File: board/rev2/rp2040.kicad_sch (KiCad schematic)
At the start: 33 parts, among them J8 Conn_01x03, U13 TLV74311, U5 RP2354B, Y1 ABM8-272-T3

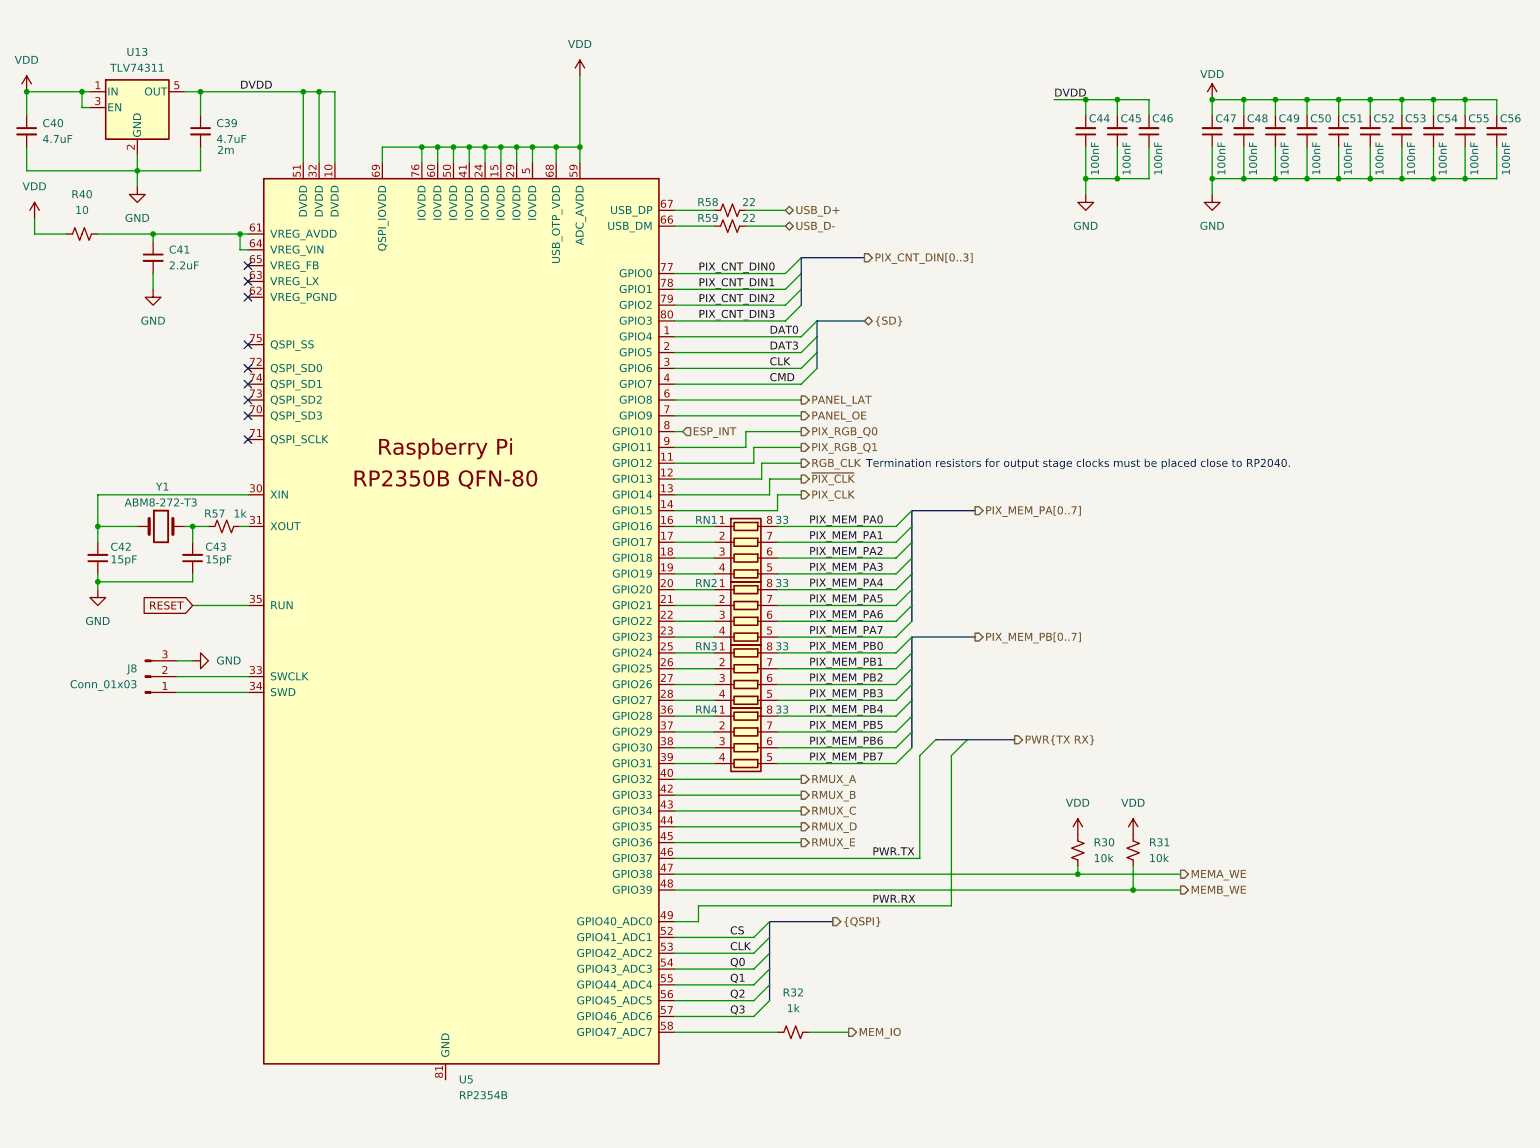
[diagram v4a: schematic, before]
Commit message: Start new PCB
- all footprints setup
- need to setup netclasses next, tho
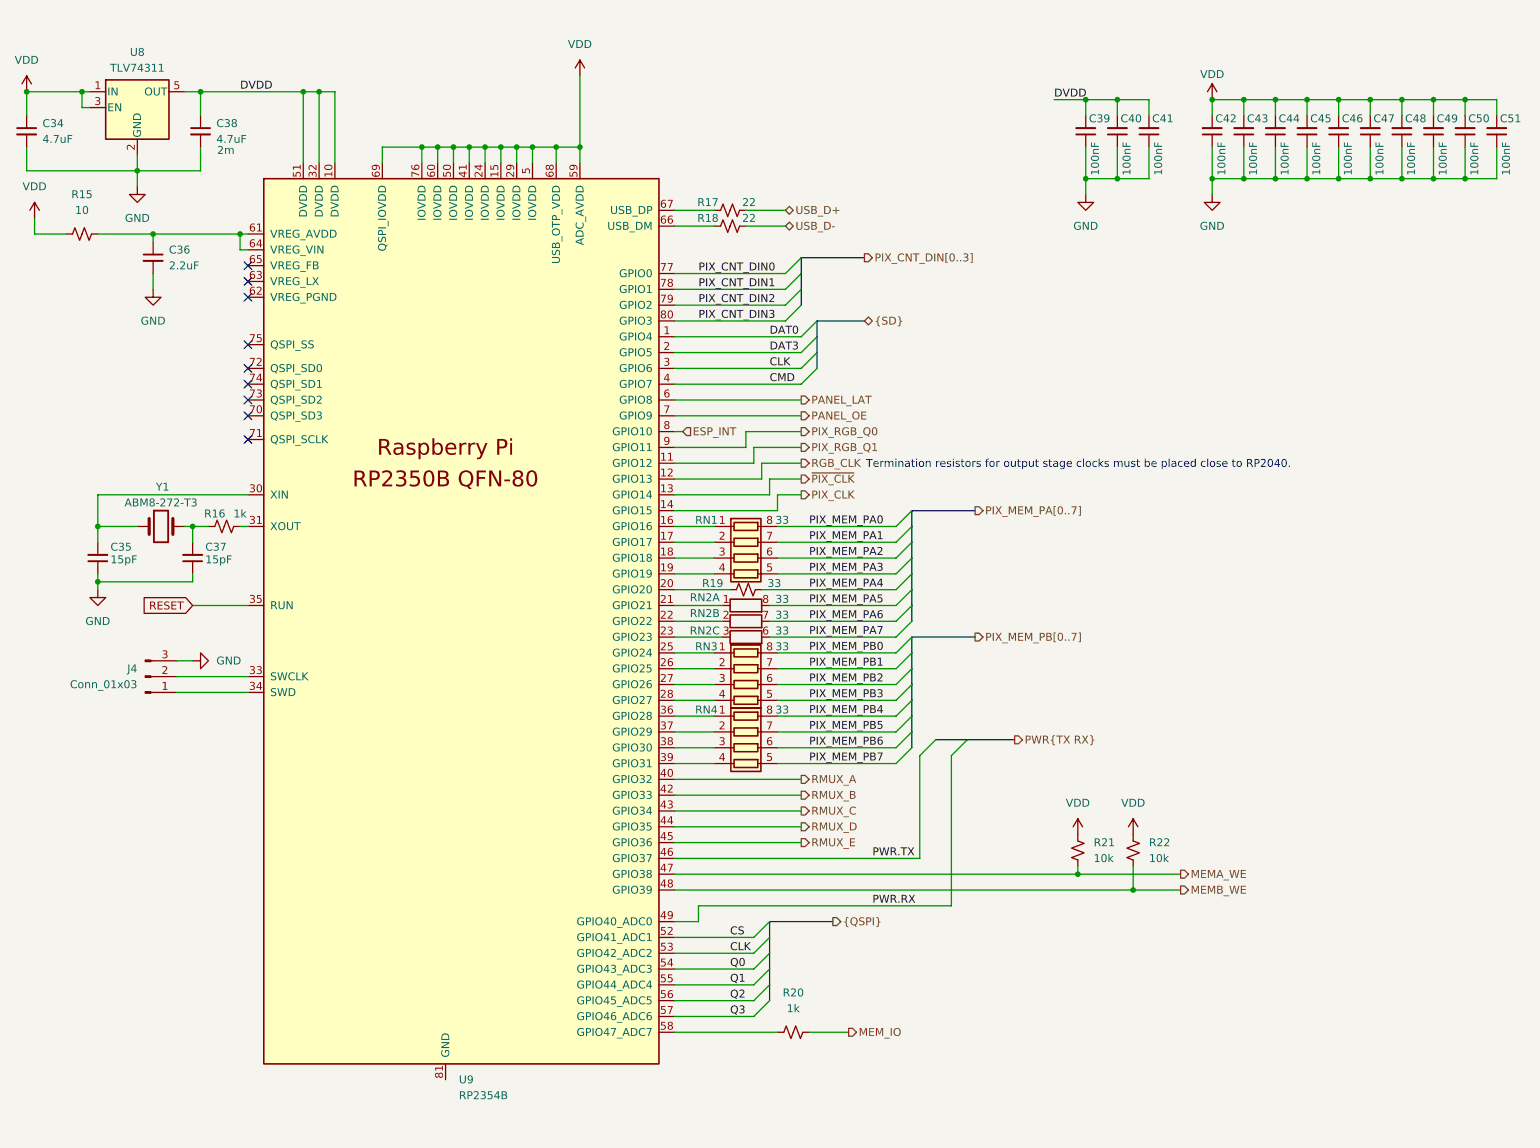
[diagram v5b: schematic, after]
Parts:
- removed RN2: 33, symbol Device:R_Pack04
- added R19: 33, Resistor_SMD:R_0402_1005Metric, symbol Device:R_Small_US
- added RN2: 33, RN_SMD:R_Array_Flat_4x0201, symbol Device:R_Pack04_Split
- RN1, RN3, RN4: footprint (none) -> RN_SMD:R_Array_Flat_4x0201; Part (none) -> YC104-FR-0733RL
- U8: renamed from U13; Part (none) -> TLV74311
- U9: renamed from U5; Part (none) -> RP2354B
- Y1: Part (none) -> ABM8-272-T3
- renumbered C40 to C34, C42 to C35, C41 to C36, C43 to C37, C39 to C38, C44 to C39, C45 to C40, C46 to C41, C47 to C42, C48 to C43, C49 to C44, C50 to C45, C51 to C46, C52 to C47, C53 to C48, C54 to C49, C55 to C50, C56 to C51, J8 to J4, R40 to R15, R57 to R16, R58 to R17, R59 to R18, R32 to R20, R30 to R21, R31 to R22
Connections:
- net PIX_MEM_PA4: now also R19.2
- net PIX_MEM_PA5: now also RN2.8 (R1.2)
- net PIX_MEM_PA6: now also RN2.7 (R2.2)
- net PIX_MEM_PA7: now also RN2.6 (R3.2)
- net at U9.20 (GPIO20): now also R19.1
- net at U9.21 (GPIO21): now also RN2.1 (R1.1)
- net at U9.22 (GPIO22): now also RN2.2 (R2.1)
- net at U9.23 (GPIO23): now also RN2.3 (R3.1)

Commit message: Add netclasses, more footprints, fix ERC
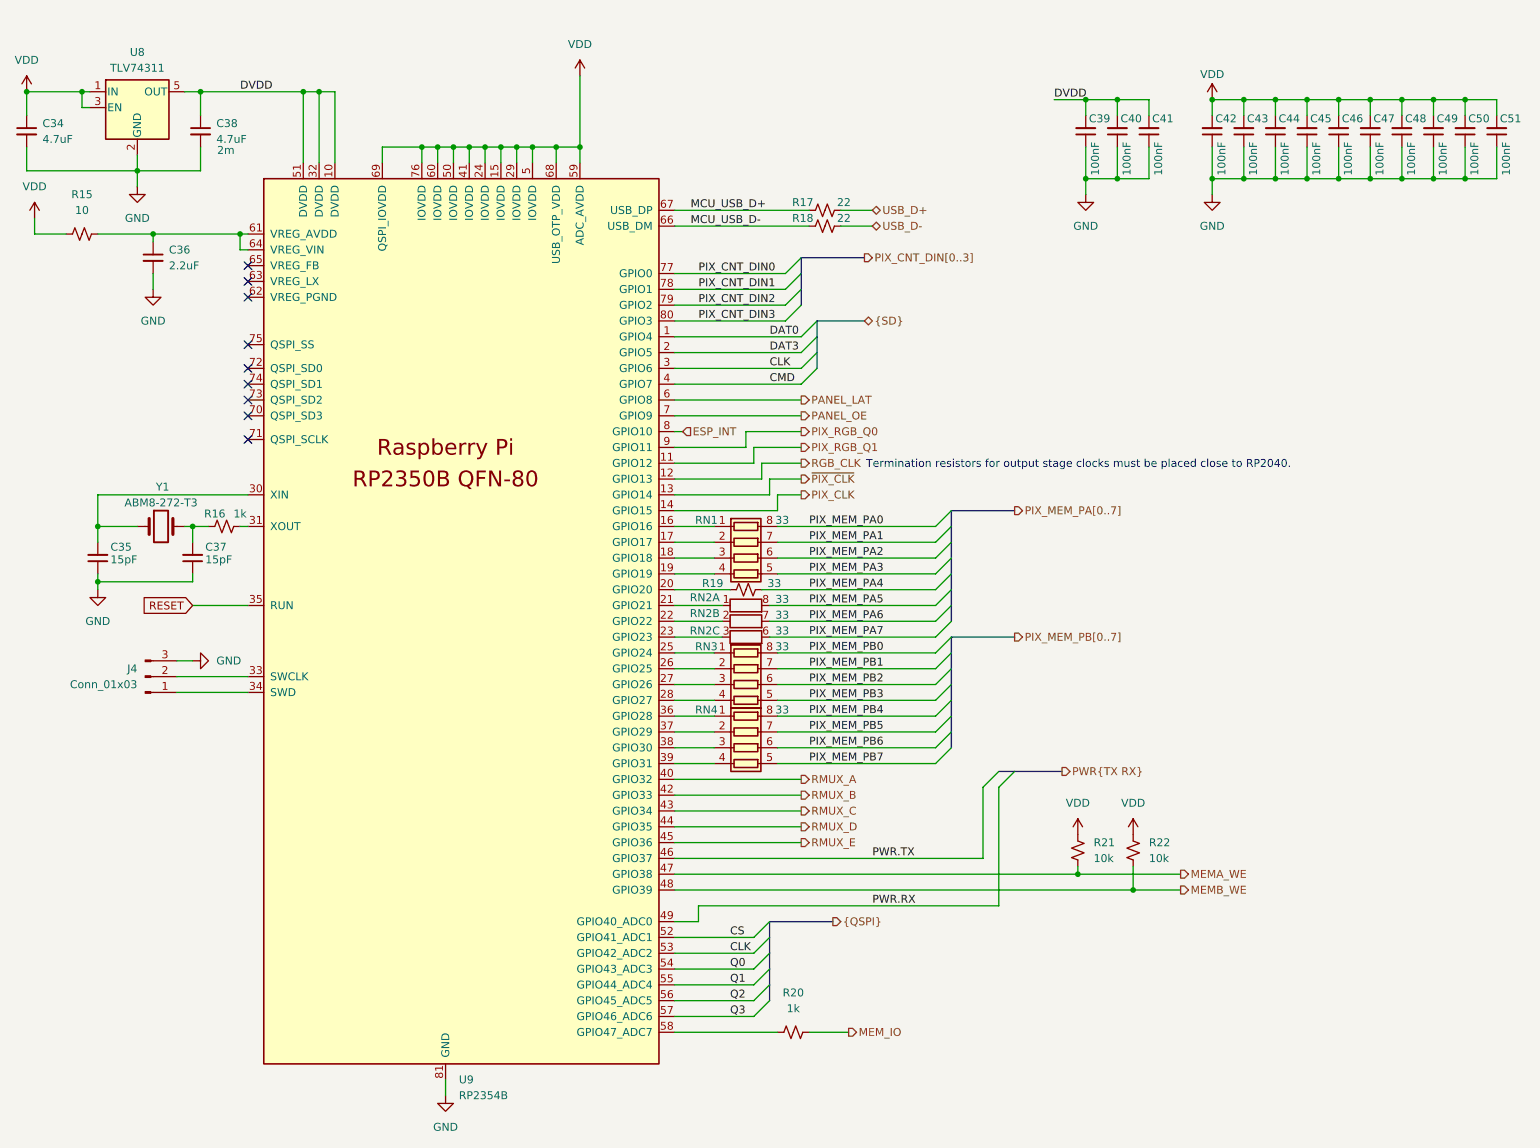
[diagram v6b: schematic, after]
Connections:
- net GND: now also U9.81 (GND)
- net MCU_USB_D+: now reaches R17.1, U9.67 (USB_DP)
- net MCU_USB_D-: now reaches R18.1, U9.66 (USB_DM)
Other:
- moved on the sheet: R17, R18

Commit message: Really finish rev2 board schematic
- fix some more footprints
  - move to real SD card holder, for example
- repair part numbers
- add LCSC part refs to everything
- add even more caps to the 3.3V reg output
  - really should use an LDO but meh it should be fine

total BOM cost for 5 of them is apparently 160 CAD, or like 32 dollars
each (don't think that includes the feeder fees tho)
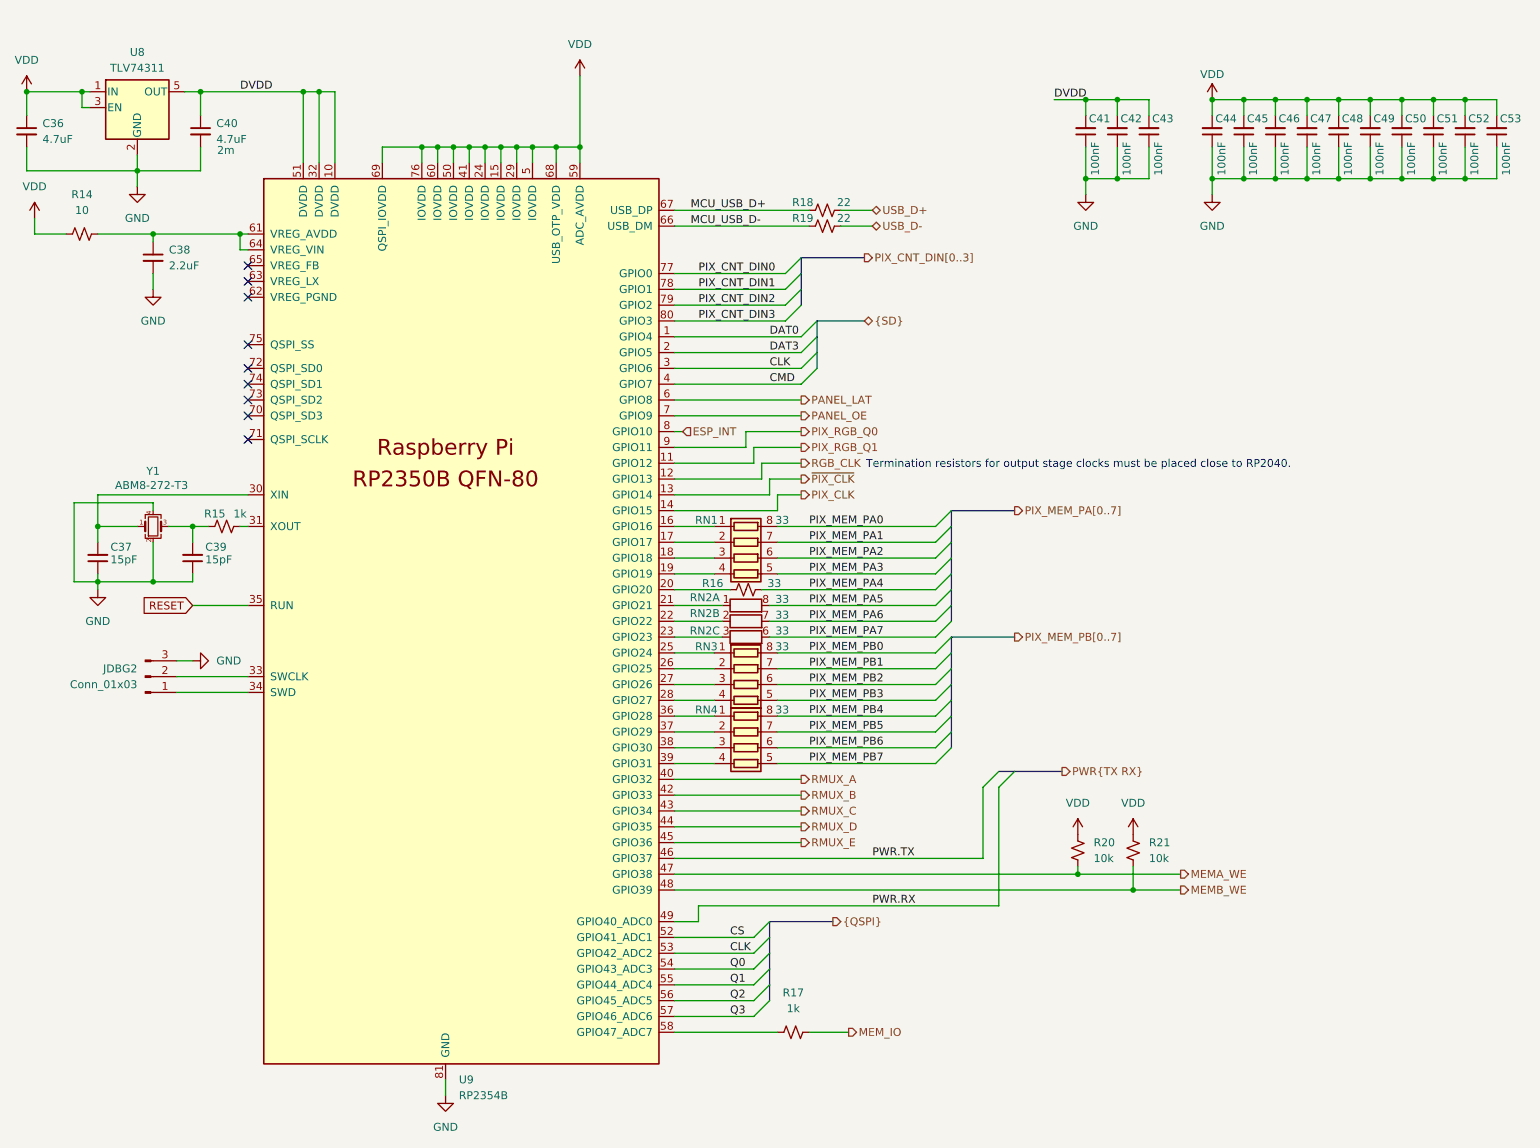
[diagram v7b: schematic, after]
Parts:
- C36: renamed from C34; LCSC (none) -> C29823
- C37: renamed from C35; LCSC (none) -> C1548
- C38: renamed from C36; LCSC (none) -> C23630
- C39: renamed from C37; LCSC (none) -> C1548
- C40: renamed from C38; LCSC (none) -> C29823
- C41: renamed from C39; LCSC (none) -> C307331
- C42: renamed from C40; LCSC (none) -> C307331
- C43: renamed from C41; LCSC (none) -> C307331
- C44: renamed from C42; LCSC (none) -> C307331
- C45: renamed from C43; LCSC (none) -> C307331
- C46: renamed from C44; LCSC (none) -> C307331
- C47: renamed from C45; LCSC (none) -> C307331
- C48: renamed from C46; LCSC (none) -> C307331
- C49: renamed from C47; LCSC (none) -> C307331
- C50: renamed from C48; LCSC (none) -> C307331
- C51: renamed from C49; LCSC (none) -> C307331
- C52: renamed from C50; LCSC (none) -> C307331
- C53: renamed from C51; LCSC (none) -> C307331
- R14: renamed from R15; LCSC (none) -> C25077
- R15: renamed from R16; LCSC (none) -> C11702
- R16: renamed from R19; LCSC (none) -> C25105
- R17: renamed from R20; LCSC (none) -> C11702
- R18: renamed from R17; LCSC (none) -> C25092
- R19: renamed from R18; LCSC (none) -> C25092
- R20: renamed from R21; LCSC (none) -> C17414
- R21: renamed from R22; LCSC (none) -> C17414
- RN1, RN2, RN3, RN4: LCSC (none) -> C854640
- U8: LCSC (none) -> C485147; Part TLV74311 -> TLV74311PDBVR
- U9: LCSC (none) -> C39843328
- Y1: symbol Device:Crystal -> Device:Crystal_GND24_Small; LCSC (none) -> C20625731
- renumbered J4 to JDBG2
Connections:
- net GND: now also Y1.2, Y1.4
- net at C39.2, R15.1: now also Y1.3; no longer Y1.2

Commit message: Start board
add a few extra bypass caps too, and swap some pins on the USB mux

i forgot to add a bypass cap on the tpd6s so that also needs to happen

truly 63 capacitors is not enough
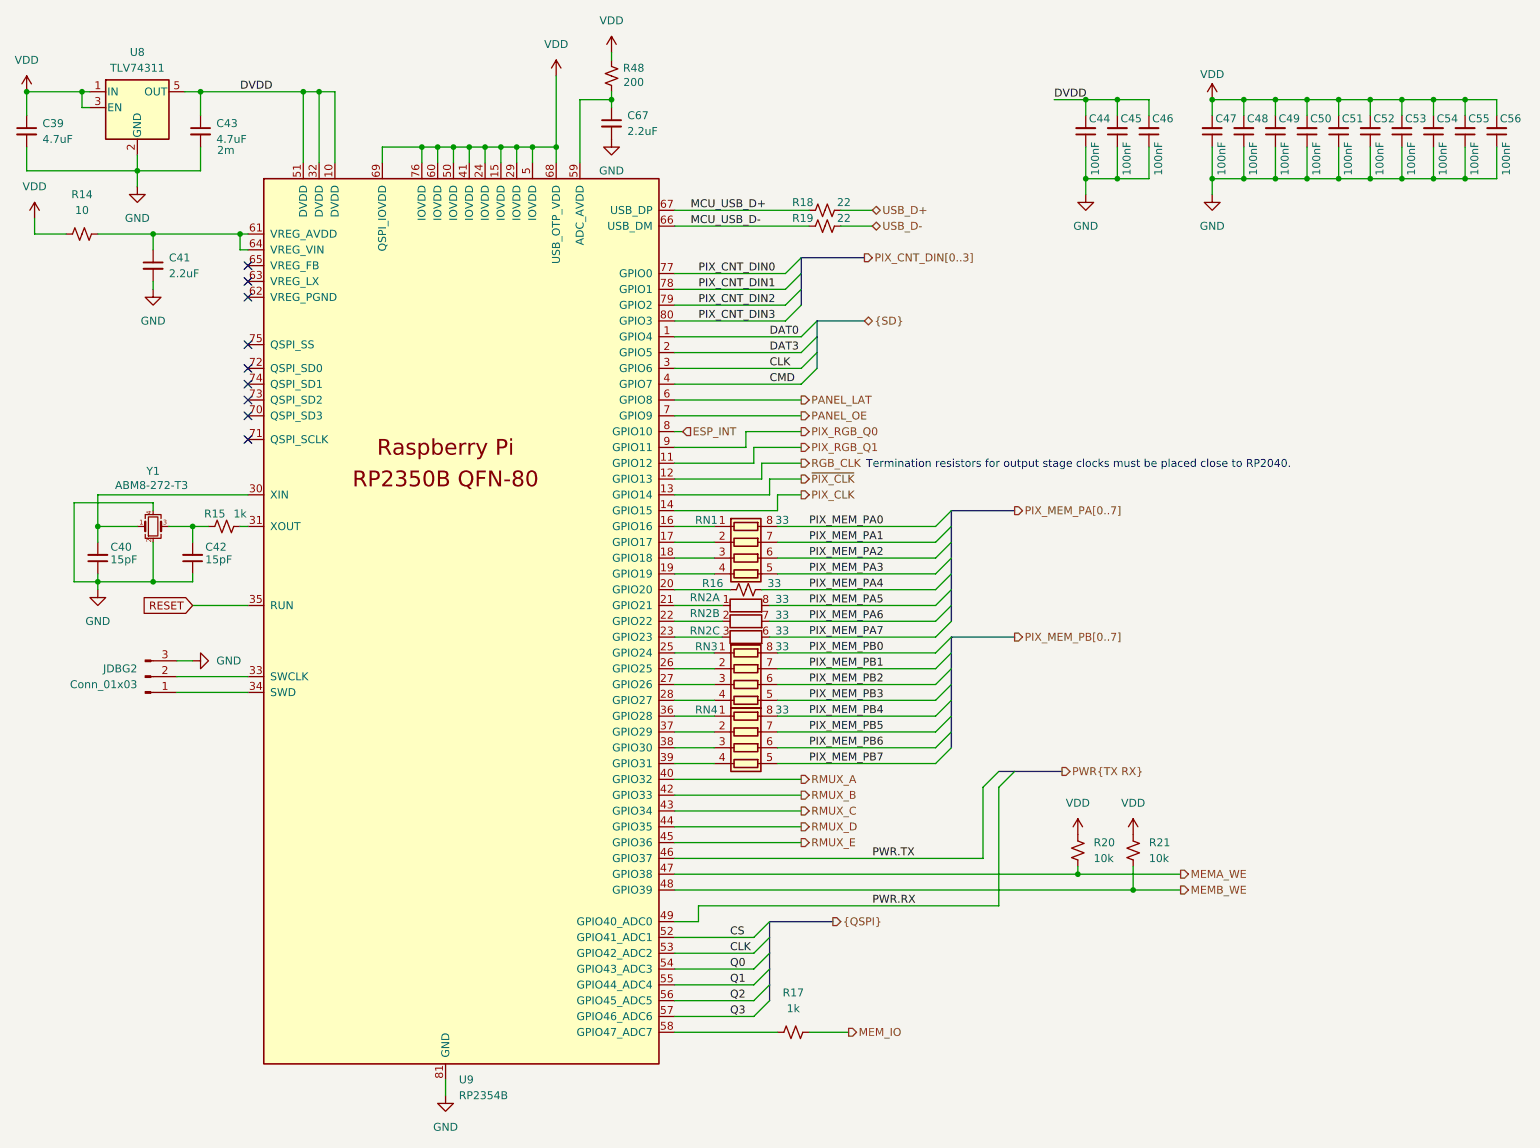
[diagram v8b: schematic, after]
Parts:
- added C67: 2.2uF, Capacitor_SMD:C_0603_1608Metric, symbol Device:C_Small
- added R48: 200, Resistor_SMD:R_0402_1005Metric, symbol Device:R_Small_US
- renumbered C36 to C39, C37 to C40, C38 to C41, C39 to C42, C40 to C43, C41 to C44, C42 to C45, C43 to C46, C44 to C47, C45 to C48, C46 to C49, C47 to C50, C48 to C51, C49 to C52, C50 to C53, C51 to C54, C52 to C55, C53 to C56
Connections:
- net GND: now also C67.2
- net VDD: now also R48.1; no longer U9.59 (ADC_AVDD)
- new net: C67.1, R48.2, U9.59 (ADC_AVDD)
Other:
- moved on the sheet: C41
